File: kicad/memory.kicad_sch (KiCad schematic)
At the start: 6 parts, among them U4 AT28C256, U5 AS6C4008, U6 62256

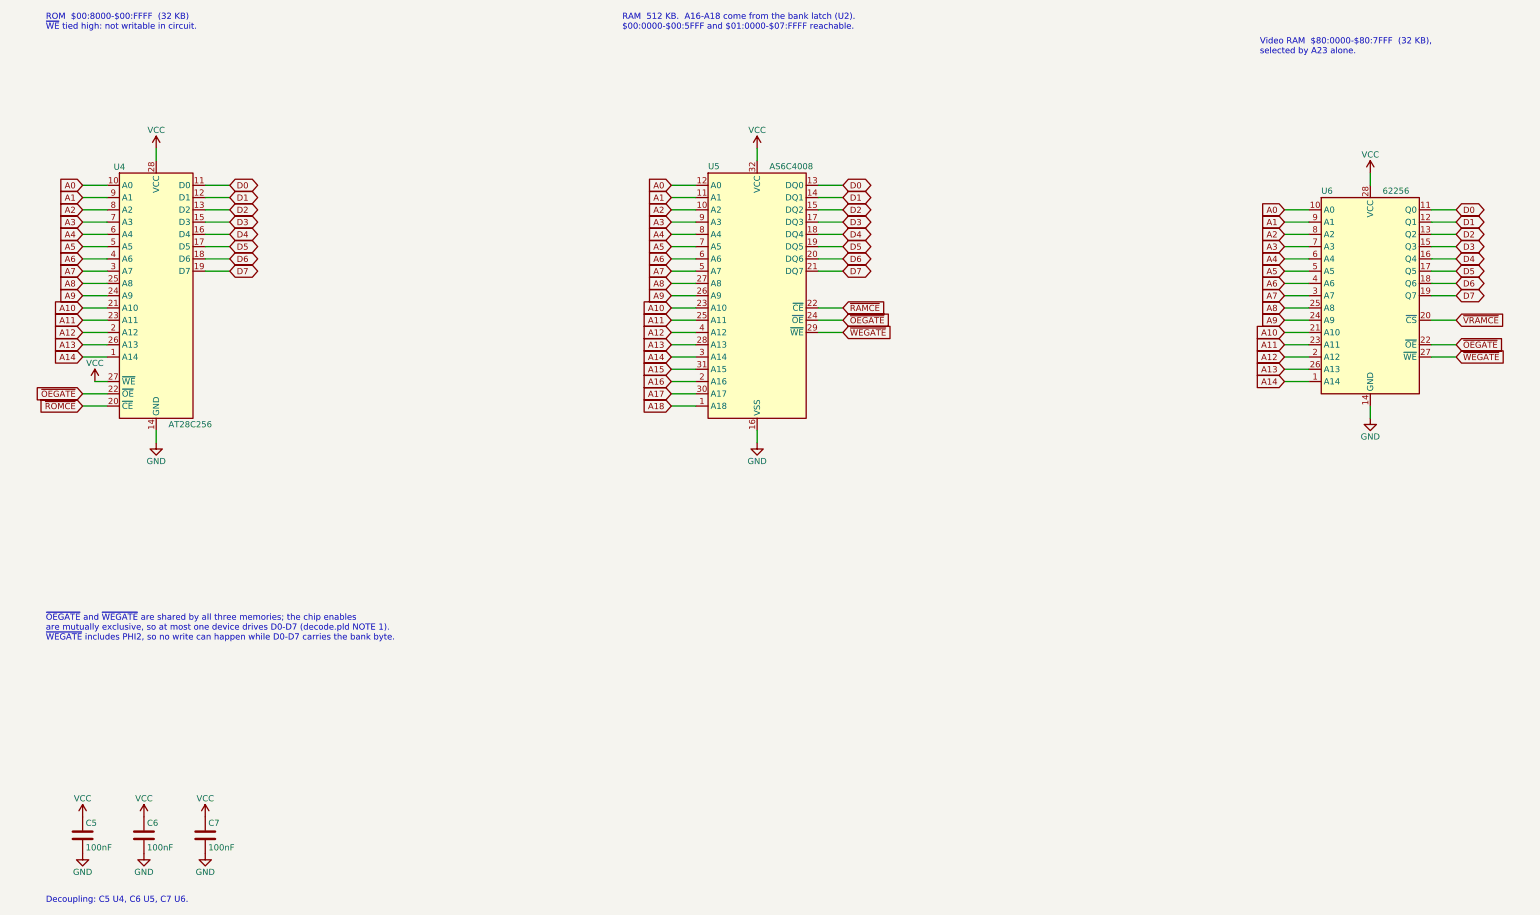
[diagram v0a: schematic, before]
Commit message: Update KiCad schematic to match the build as wired
- Remove video RAM (future expansion); GAL ~{VRAMCE} is NC and
  ~{WEGATE} goes only to the RAM
- VIA is a W65C22N6TPG-14: IRQB wired directly to ~{IRQ} (no diode)
- RDY and ~{NMI} tied directly to +5V; only reset and ~{IRQ} pull-ups
- ACIA clocked by a 1.8432 MHz DIP-8 oscillator on XTLI (EN high)
- Serial through a MAX232N to a female DB9 (pins 2, 3, 8, 5)
- VIA Port B drives eight LEDs with series resistors; Port A, CA/CB NC
- Drop per-chip decoupling; single 0.1uF electrolytic at the supply
- Unknown resistor values shown as '?'
- Update kicad/README.md and README.md accordingly

Co-Authored-By: Claude Opus 5.5 <noreply@anthropic.com>
Claude-Session: https://claude.ai/code/session_01GgTWzZQQJPzWrEMiSDZH6j
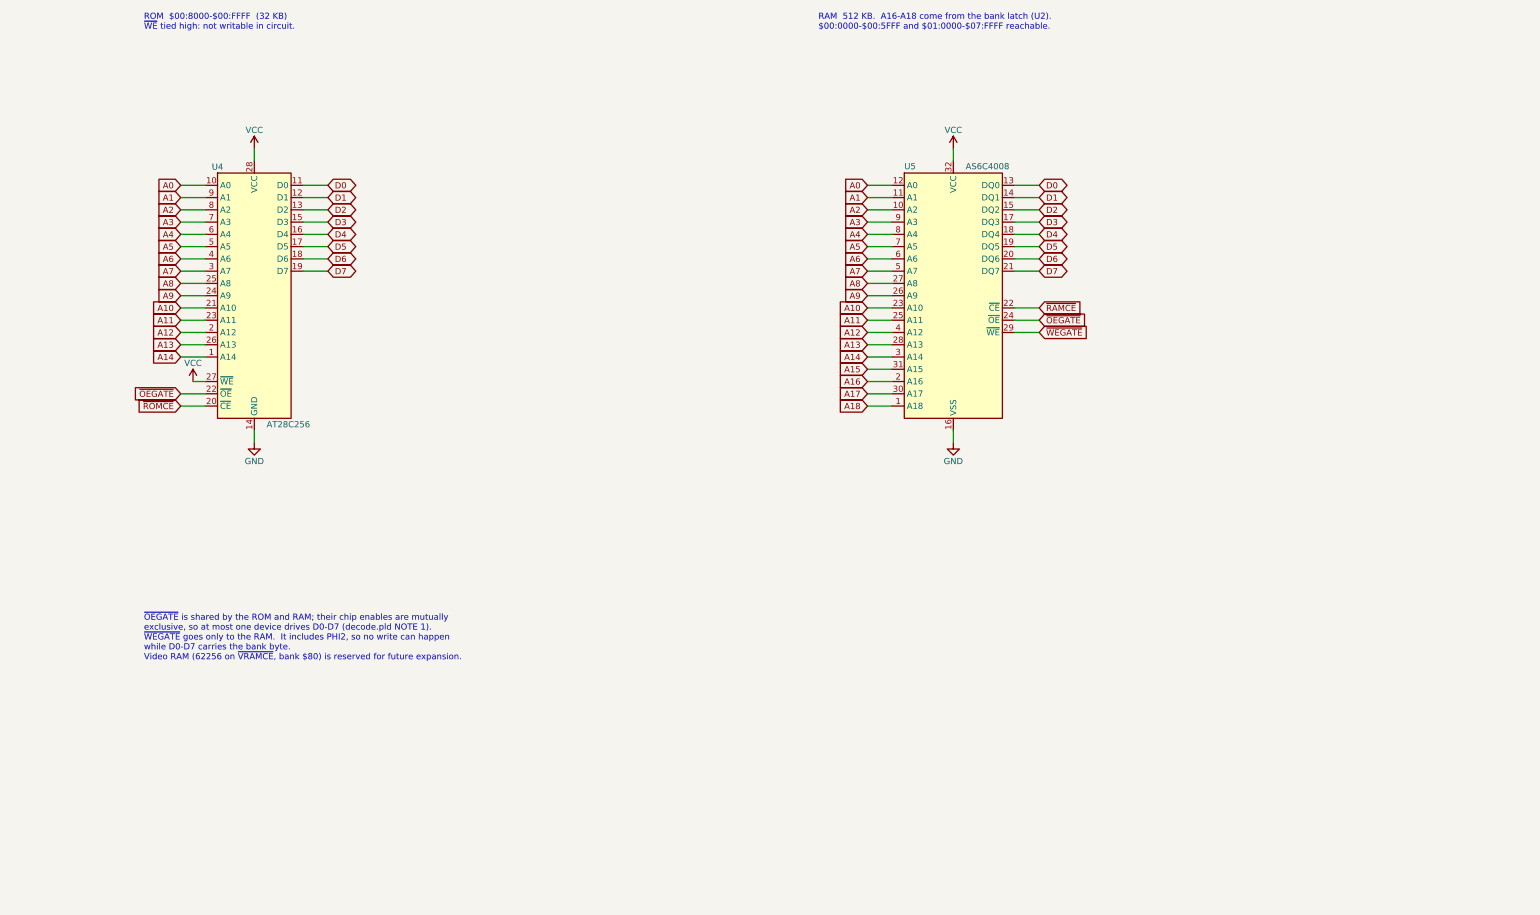
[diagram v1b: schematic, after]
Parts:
- removed C5, C6, C7: 100nF, symbol be6502:C
- removed U6: 62256, Package_DIP:DIP-28_W15.24mm, symbol be6502:62256
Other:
- note added: "~{OEGATE} is shared by the ROM and RAM; their chip enables are mutually exclusive, so at most one device drives D0-D7 (decode.pld NOTE 1). ~{WEGATE} goes only to the RAM. It includes PHI2, so no write can happen while D0-D7 carries the bank byte. Video RAM (62256 on ~{VRAMCE}, bank $80) is reserved for future expansion."
- note removed: "Decoupling: C5 U4, C6 U5, C7 U6."
- note removed: "Video RAM $80:0000-$80:7FFF (32 KB), selected by A23 alone."
- note removed: "~{OEGATE} and ~{WEGATE} are shared by all three memories; the chip enables are mutually exclusive, so at most one device drives D0-D7 (decode.pld NOTE 1). ~{WEGATE} includes PHI2, so no write can happen while D0-D7 carries the bank byte."
- title: Memory: ROM, RAM, video RAM -> Memory: ROM and RAM

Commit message: Schematic rev 2: prepare the design for a 4-layer PCB
Keeps the breadboard's parts and logic and adds what a board needs.

- RDY, NMI, ABORT and BE get 3.3k pull-ups instead of hard ties to +5V
  (RDY is bidirectional; WAI drives it low).
- VDA and VPA go to GAL pins 11 and 13. New pld/decode03.pld (816DEC03)
  qualifies /IOSEL with VDA + VPA so internal-operation cycles cannot
  read and clear ACIA/VIA registers. decode.pld (816DEC02) stays for the
  breadboard.
- PHI2 from the GAL can be routed through a 74ACT08 buffer via JP2
  (default: direct, as built). Timing in decode03.pld NOTE 8.
- Clock source jumper JP1 and external clock header J5.
- New power sheet: USB-C (power only) or bench terminal via JP4, power
  switch, polyfuse, P-FET reverse-polarity protection, 47uF bulk, power
  LED, and 100nF decoupling per package.
- New expansion sheet: 2x30 bus header (address, latched bank byte,
  data, control, spare I/O slots), 2x12 VIA header, LED disconnect
  jumper, test points, mounting holes.
- Footprints on every part; socket footprints for all ICs.

ERC (KiCad 9.0.4 kicad-cli): 0 errors, 0 warnings. Both PLD files
assemble with Galette 0.3.0.

Co-Authored-By: Claude Opus 5.5 <noreply@anthropic.com>
Claude-Session: https://claude.ai/code/session_01WF6ESyzfg6uQED2DRD2W4Z
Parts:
- U4: footprint Package_DIP:DIP-28_W15.24mm -> Package_DIP:DIP-28_W15.24mm_Socket
- U5: footprint Package_DIP:DIP-32_W15.24mm -> Package_DIP:DIP-32_W15.24mm_Socket
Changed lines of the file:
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@@
 (kicad_sch (version 20230121) (generator eeschema)
 (paper "A3")
-(title_block (title "Memory: ROM and RAM") (date "2026-10-16") (rev "1") (company "be6502") (comment 1 "W65C816S breadboard computer - see README.md and pld/decode.pld") (comment 2 "Active-low signals use KiCad overbar notation, e.g. ~{IOSEL}"))
-(symbol (lib_id "be6502:AT28C256") (at 101.6 109.22 0) (unit 1) (in_bom yes) (on_board yes) (dnp no) (property "Reference" "U4" (at 93.98 82.55 0) (effects (font (size 1.27 1.27)))) (property "Value" "AT28C256" (at 104.14 135.89 0) (effects (font (size 1.27 1.27)) (justify left))) (property "Footprint" "Package_DIP:DIP-28_W15.24mm" (at 101.6 109.22 0) (effects (font (size 1.27 1.27)) hide)) (property "Datasheet" "http://ww1.microchip.com/downloads/en/DeviceDoc/doc0006.pdf" (at 101.6 109.22 0) (effects (font (size 1.27 1.27)) hide)) (pin "1") (pin "10") (pin "11") (pin "12") (pin "13") (pin "14") (pin "15") (pin "16") (pin "17") (pin "18") (pin "19") (pin "2") (pin "20") (pin "21") (pin "22") (pin "23") (pin "24") (pin "25") (pin "26") (pin "27") (pin "28") (pin "3") (pin "4") (pin "5") (pin "6") (pin "7") (pin "8") (pin "9") (instances (project "be6502" (path "/c8451a90-6bbf-595d-a4c9-ea2cdd0996a1/9143e839-df6e-52bf-a121-3a9a8f1625cb" (reference "U4") (unit 1)))))
+(title_block (title "Memory: ROM and RAM") (date "2026-10-16") (rev "2") (company "be6502") (comment 1 "W65C816S breadboard computer - see README.md and pld/decode.pld") (comment 2 "Active-low signals use KiCad overbar notation, e.g. ~{IOSEL}"))
+(symbol (lib_id "be6502:AT28C256") (at 101.6 109.22 0) (unit 1) (in_bom yes) (on_board yes) (dnp no) (property "Reference" "U4" (at 93.98 82.55 0) (effects (font (size 1.27 1.27)))) (property "Value" "AT28C256" (at 104.14 135.89 0) (effects (font (size 1.27 1.27)) (justify left))) (property "Footprint" "Package_DIP:DIP-28_W15.24mm_Socket" (at 101.6 109.22 0) (effects (font (size 1.27 1.27)) hide)) (property "Datasheet" "http://ww1.microchip.com/downloads/en/DeviceDoc/doc0006.pdf" (at 101.6 109.22 0) (effects (font (size 1.27 1.27)) hide)) (pin "1") (pin "10") (pin "11") (pin "12") (pin "13") (pin "14") (pin "15") (pin "16") (pin "17") (pin "18") (pin "19") (pin "2") (pin "20") (pin "21") (pin "22") (pin "23") (pin "24") (pin "25") (pin "26") (pin "27") (pin "28") (pin "3") (pin "4") (pin "5") (pin "6") (pin "7") (pin "8") (pin "9") (instances (project "be6502" (path "/c8451a90-6bbf-595d-a4c9-ea2cdd0996a1/9143e839-df6e-52bf-a121-3a9a8f1625cb" (reference "U4") (unit 1)))))
 (wire (pts (xy 91.44 132.08) (xy 86.36 132.08)) (stroke (width 0) (type default)))
 (global_label "~{ROMCE}" (shape input) (at 86.36 132.08 180) (fields_autoplaced) (effects (font (size 1.27 1.27)) (justify right)) (property "Intersheetrefs" "${INTERSHEET_REFS}" (at 86.36 132.08 0) (effects (font (size 1.27 1.27)) (justify right) hide)))
@@
 (symbol (lib_id "be6502:VCC") (at 88.9 127 0) (unit 1) (in_bom no) (on_board no) (dnp no) (property "Reference" "#PWR016" (at 88.9 130.81 0) (effects (font (size 1.27 1.27)) hide)) (property "Value" "VCC" (at 88.9 123.19 0) (effects (font (size 1.27 1.27)))) (property "Footprint" "" (at 88.9 127 0) (effects (font (size 1.27 1.27)) hide)) (property "Datasheet" "" (at 88.9 127 0) (effects (font (size 1.27 1.27)) hide)) (pin "1") (instances (project "be6502" (path "/c8451a90-6bbf-595d-a4c9-ea2cdd0996a1/9143e839-df6e-52bf-a121-3a9a8f1625cb" (reference "#PWR016") (unit 1)))))
 (text "ROM  $00:8000-$00:FFFF  (32 KB)\n~{WE} tied high: not writable in circuit." (at 78.74 50.8 0) (effects (font (size 1.27 1.27)) (justify left top)))
-(symbol (lib_id "be6502:AS6C4008") (at 246.38 109.22 0) (unit 1) (in_bom yes) (on_board yes) (dnp no) (property "Reference" "U5" (at 236.22 83.185 0) (effects (font (size 1.27 1.27)) (justify left bottom))) (property "Value" "AS6C4008" (at 248.92 83.185 0) (effects (font (size 1.27 1.27)) (justify left bottom))) (property "Footprint" "Package_DIP:DIP-32_W15.24mm" (at 246.38 106.68 0) (effects (font (size 1.27 1.27)) hide)) (property "Datasheet" "https://www.alliancememory.com/wp-content/uploads/pdf/AS6C4008.pdf" (at 246.38 106.68 0) (effects (font (size 1.27 1.27)) hide)) (pin "16") (pin "32") (pin "1") (pin "10") (pin "11") (pin "12") (pin "13") (pin "14") (pin "15") (pin "17") (pin "18") (pin "19") (pin "2") (pin "20") (pin "21") (pin "22") (pin "23") (pin "24") (pin "25") (pin "26") (pin "27") (pin "28") (pin "29") (pin "3") (pin "30") (pin "31") (pin "4") (pin "5") (pin "6") (pin "7") (pin "8") (pin "9") (instances (project "be6502" (path "/c8451a90-6bbf-595d-a4c9-ea2cdd0996a1/9143e839-df6e-52bf-a121-3a9a8f1625cb" (reference "U5") (unit 1)))))
+(symbol (lib_id "be6502:AS6C4008") (at 246.38 109.22 0) (unit 1) (in_bom yes) (on_board yes) (dnp no) (property "Reference" "U5" (at 236.22 83.185 0) (effects (font (size 1.27 1.27)) (justify left bottom))) (property "Value" "AS6C4008" (at 248.92 83.185 0) (effects (font (size 1.27 1.27)) (justify left bottom))) (property "Footprint" "Package_DIP:DIP-32_W15.24mm_Socket" (at 246.38 106.68 0) (effects (font (size 1.27 1.27)) hide)) (property "Datasheet" "https://www.alliancememory.com/wp-content/uploads/pdf/AS6C4008.pdf" (at 246.38 106.68 0) (effects (font (size 1.27 1.27)) hide)) (pin "16") (pin "32") (pin "1") (pin "10") (pin "11") (pin "12") (pin "13") (pin "14") (pin "15") (pin "17") (pin "18") (pin "19") (pin "2") (pin "20") (pin "21") (pin "22") (pin "23") (pin "24") (pin "25") (pin "26") (pin "27") (pin "28") (pin "29") (pin "3") (pin "30") (pin "31") (pin "4") (pin "5") (pin "6") (pin "7") (pin "8") (pin "9") (instances (project "be6502" (path "/c8451a90-6bbf-595d-a4c9-ea2cdd0996a1/9143e839-df6e-52bf-a121-3a9a8f1625cb" (reference "U5") (unit 1)))))
 (wire (pts (xy 259.08 111.76) (xy 264.16 111.76)) (stroke (width 0) (type default)))
 (global_label "~{RAMCE}" (shape input) (at 264.16 111.76 0) (fields_autoplaced) (effects (font (size 1.27 1.27)) (justify left)) (property "Intersheetrefs" "${INTERSHEET_REFS}" (at 264.16 111.76 0) (effects (font (size 1.27 1.27)) (justify left) hide)))
